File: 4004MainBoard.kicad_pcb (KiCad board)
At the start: 2 copper layers, 95.1 x 72.1 mm, 99 parts, among them J1 BUS, J2 P0 RAM1, J3 CMRAM RAM2, J4 P0 RAM2, J5 DC 5V, Q1 2SA1162GR, Q10 2SC2712GR, Q11 2SA1162GR, Q2 2SC2712GR, Q3 2SA1162GR, Q4 2SC2712GR, Q5 2SA1162GR, Q6 2SA1162GR, Q7 2SA1162GR, Q8 2SA1162GR, Q9 2SC2712GR, SW1 TEST, SW2 RESET, SW3 POWER, U1 74HC08, U2 74HC161, U3 PST600, U4 Intel4004, U5 LT1931A, U6 74LS540, U7 Intel4002-1, U8 Intel4002-1, U9 LT1763, Y1 DLO555MB

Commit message: パターン修正 ビア実装
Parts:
- added R29: 22, Resistors_SMD:R_0603_HandSoldering, B.Cu at (162.1, 111.3)
- added R30: 22, Resistors_SMD:R_0603_HandSoldering, B.Cu at (168.0, 106.4)
- added R31: 22k, Resistors_SMD:R_0603_HandSoldering, B.Cu at (179.3, 101.6)
- added R32: 22k, Resistors_SMD:R_0603_HandSoldering, B.Cu at (198.6, 101.3)
- added R33: 22k, Resistors_SMD:R_0603_HandSoldering, B.Cu at (200.7, 100.7)
- added R34: 22k, Resistors_SMD:R_0603_HandSoldering, B.Cu at (193.4, 101.7)
- added REF**: VIA-0.8-Hole-0.4mm, cd_device:VIA-0.8-Hole-0.4mm, F.Cu at (150.7, 114.2)
- added REF**: VIA-0.8-Hole-0.4mm, cd_device:VIA-0.8-Hole-0.4mm, F.Cu at (157.9, 127.8)
- added REF**: VIA-0.8-Hole-0.4mm, cd_device:VIA-0.8-Hole-0.4mm, F.Cu at (169.9, 134.9)
- added REF**: VIA-0.8-Hole-0.4mm, cd_device:VIA-0.8-Hole-0.4mm, F.Cu at (170.1, 126.1)
- added REF**: VIA-0.8-Hole-0.4mm, cd_device:VIA-0.8-Hole-0.4mm, F.Cu at (168.4, 121.5)
- added REF**: VIA-0.8-Hole-0.4mm, cd_device:VIA-0.8-Hole-0.4mm, F.Cu at (176.4, 137.4)
- added REF**: VIA-0.8-Hole-0.4mm, cd_device:VIA-0.8-Hole-0.4mm, F.Cu at (132.8, 125.7)
- added REF**: VIA-0.8-Hole-0.4mm, cd_device:VIA-0.8-Hole-0.4mm, F.Cu at (142.6, 141.9)
- added REF**: VIA-0.8-Hole-0.4mm, cd_device:VIA-0.8-Hole-0.4mm, F.Cu at (153.3, 133.5)
- added REF**: VIA-0.8-Hole-0.4mm, cd_device:VIA-0.8-Hole-0.4mm, F.Cu at (149.1, 117.6)
- added REF**: VIA-0.8-Hole-0.4mm, cd_device:VIA-0.8-Hole-0.4mm, F.Cu at (146.2, 96.4)
- added REF**: VIA-0.8-Hole-0.4mm, cd_device:VIA-0.8-Hole-0.4mm, F.Cu at (150.7, 138.7)
- added REF**: VIA-0.8-Hole-0.4mm, cd_device:VIA-0.8-Hole-0.4mm, F.Cu at (150.0, 100.2)
- added REF**: VIA-0.8-Hole-0.4mm, cd_device:VIA-0.8-Hole-0.4mm, F.Cu at (139.2, 105.8)
- added REF**: VIA-0.8-Hole-0.4mm, cd_device:VIA-0.8-Hole-0.4mm, F.Cu at (145.7, 85.6)
- added REF**: VIA-0.8-Hole-0.4mm, cd_device:VIA-0.8-Hole-0.4mm, F.Cu at (156.8, 95.4)
- added REF**: VIA-0.8-Hole-0.4mm, cd_device:VIA-0.8-Hole-0.4mm, F.Cu at (174.6, 101.2)
- added REF**: VIA-0.8-Hole-0.4mm, cd_device:VIA-0.8-Hole-0.4mm, F.Cu at (164.3, 95.1)
- added REF**: VIA-0.8-Hole-0.4mm, cd_device:VIA-0.8-Hole-0.4mm, F.Cu at (162.2, 79.5)
- added REF**: VIA-0.8-Hole-0.4mm, cd_device:VIA-0.8-Hole-0.4mm, F.Cu at (208.3, 81.3)
- added REF**: VIA-0.8-Hole-0.4mm, cd_device:VIA-0.8-Hole-0.4mm, F.Cu at (203.5, 90.7)
- added REF**: VIA-0.8-Hole-0.4mm, cd_device:VIA-0.8-Hole-0.4mm, F.Cu at (196.8, 85.2)
- added REF**: VIA-0.8-Hole-0.4mm, cd_device:VIA-0.8-Hole-0.4mm, F.Cu at (148.1, 138.7)
- added REF**: VIA-0.8-Hole-0.4mm, cd_device:VIA-0.8-Hole-0.4mm, F.Cu at (180.2, 131.1)
- added REF**: VIA-0.8-Hole-0.4mm, cd_device:VIA-0.8-Hole-0.4mm, F.Cu at (225.0, 81.2)
- added REF**: VIA-0.8-Hole-0.4mm, cd_device:VIA-0.8-Hole-0.4mm, F.Cu at (218.3, 90.6)
- added REF**: VIA-0.8-Hole-0.4mm, cd_device:VIA-0.8-Hole-0.4mm, F.Cu at (172.8, 84.7)
- added REF**: VIA-0.8-Hole-0.4mm, cd_device:VIA-0.8-Hole-0.4mm, F.Cu at (204.3, 78.9)
- added REF**: VIA-0.8-Hole-0.4mm, cd_device:VIA-0.8-Hole-0.4mm, F.Cu at (193.3, 91.7)
- added REF**: VIA-0.8-Hole-0.4mm, cd_device:VIA-0.8-Hole-0.4mm, F.Cu at (215.1, 72.5)
- added REF**: VIA-0.8-Hole-0.4mm, cd_device:VIA-0.8-Hole-0.4mm, F.Cu at (190.1, 142.0)
- added REF**: VIA-0.8-Hole-0.4mm, cd_device:VIA-0.8-Hole-0.4mm, F.Cu at (225.3, 120.1)
- added REF**: VIA-0.8-Hole-0.4mm, cd_device:VIA-0.8-Hole-0.4mm, F.Cu at (225.3, 135.8)
- added REF**: VIA-0.8-Hole-0.4mm, cd_device:VIA-0.8-Hole-0.4mm, F.Cu at (145.5, 108.0)
- added REF**: VIA-0.8-Hole-0.4mm, cd_device:VIA-0.8-Hole-0.4mm, F.Cu at (196.6, 130.7)
- added REF**: VIA-0.8-Hole-0.4mm, cd_device:VIA-0.8-Hole-0.4mm, F.Cu at (219.1, 141.9)
- added REF**: VIA-0.8-Hole-0.4mm, cd_device:VIA-0.8-Hole-0.4mm, F.Cu at (223.8, 116.0)
- added REF**: VIA-0.8-Hole-0.4mm, cd_device:VIA-0.8-Hole-0.4mm, F.Cu at (212.2, 124.1)
- added REF**: VIA-0.8-Hole-0.4mm, cd_device:VIA-0.8-Hole-0.4mm, F.Cu at (214.8, 118.6)
- added REF**: VIA-0.8-Hole-0.4mm, cd_device:VIA-0.8-Hole-0.4mm, F.Cu at (205.4, 105.3)
- added REF**: VIA-0.8-Hole-0.4mm, cd_device:VIA-0.8-Hole-0.4mm, F.Cu at (207.0, 115.7)
- added REF**: VIA-0.8-Hole-0.4mm, cd_device:VIA-0.8-Hole-0.4mm, F.Cu at (185.4, 87.8)
- added REF**: VIA-0.8-Hole-0.4mm, cd_device:VIA-0.8-Hole-0.4mm, F.Cu at (175.5, 119.5)
- added REF**: VIA-0.8-Hole-0.4mm, cd_device:VIA-0.8-Hole-0.4mm, F.Cu at (182.8, 116.1)
- added REF**: VIA-0.8-Hole-0.4mm, cd_device:VIA-0.8-Hole-0.4mm, F.Cu at (140.6, 109.7)
- added REF**: VIA-0.8-Hole-0.4mm, cd_device:VIA-0.8-Hole-0.4mm, F.Cu at (196.5, 118.9)
- added REF**: VIA-0.8-Hole-0.4mm, cd_device:VIA-0.8-Hole-0.4mm, F.Cu at (145.4, 123.7)
- added REF**: VIA-0.8-Hole-0.4mm, cd_device:VIA-0.8-Hole-0.4mm, F.Cu at (141.1, 114.8)
- added REF**: VIA-0.8-Hole-0.4mm, cd_device:VIA-0.8-Hole-0.4mm, F.Cu at (139.3, 123.7)
- added REF**: VIA-0.8-Hole-0.4mm, cd_device:VIA-0.8-Hole-0.4mm, F.Cu at (147.1, 131.4)
- D12: value POWER LED -> POWER
- R13: value 10 -> 22
- moved C18 0.80 mm to (196.5, 115.3), turned to 90 degrees
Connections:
- Q2 pad 2: /CLK2 -> Net-(Q2-Pad2)
- Q4 pad 2: /CLK1 -> Net-(Q4-Pad2)
- Q5 pad 2: /CLK2 -> Net-(Q2-Pad2)
- Q6 pad 2: /CLK1 -> Net-(Q4-Pad2)
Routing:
- net GND: track 3.36 -> 30.7 mm
- net VCC: track 361.9 -> 381.3 mm, vias 8 -> 9
- net /CLK2: track 102.5 -> 93.9 mm
- net /D0: track 59.8 -> 68.0 mm
- net Net-(Q2-Pad2): track 0.00 -> 6.39 mm
- net /D1: track 66.8 -> 73.0 mm
- net Net-(C20-Pad1): track 24.9 -> 30.7 mm, vias 2 -> 3
- net Net-(Q4-Pad2): track 0.00 -> 3.50 mm
- net /D2: track 70.8 -> 74.2 mm
- net /CLK1: track 86.7 -> 84.3 mm
- net Net-(J1-Pad32): track 67.5 -> 65.6 mm
- net Net-(D1-Pad1): track 0.00 -> 1.49 mm, vias 0 -> 1
- net Net-(J1-Pad31): track 59.5 -> 58.0 mm
- net Net-(D6-Pad1): track 0.00 -> 1.33 mm, vias 0 -> 1
- net Net-(D7-Pad1): track 0.00 -> 1.32 mm, vias 0 -> 1
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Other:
- board text added: "1"

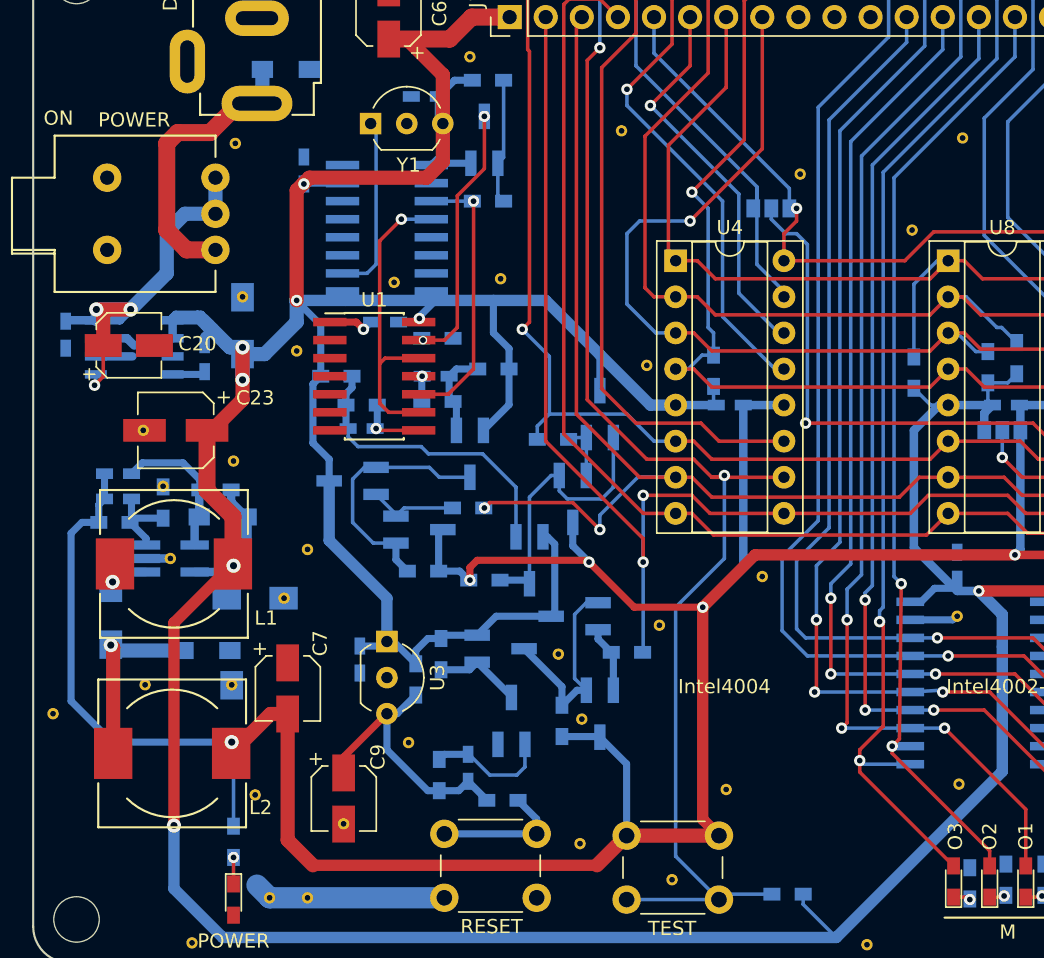
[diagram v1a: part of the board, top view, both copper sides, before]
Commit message: 回路修正 シルク修正
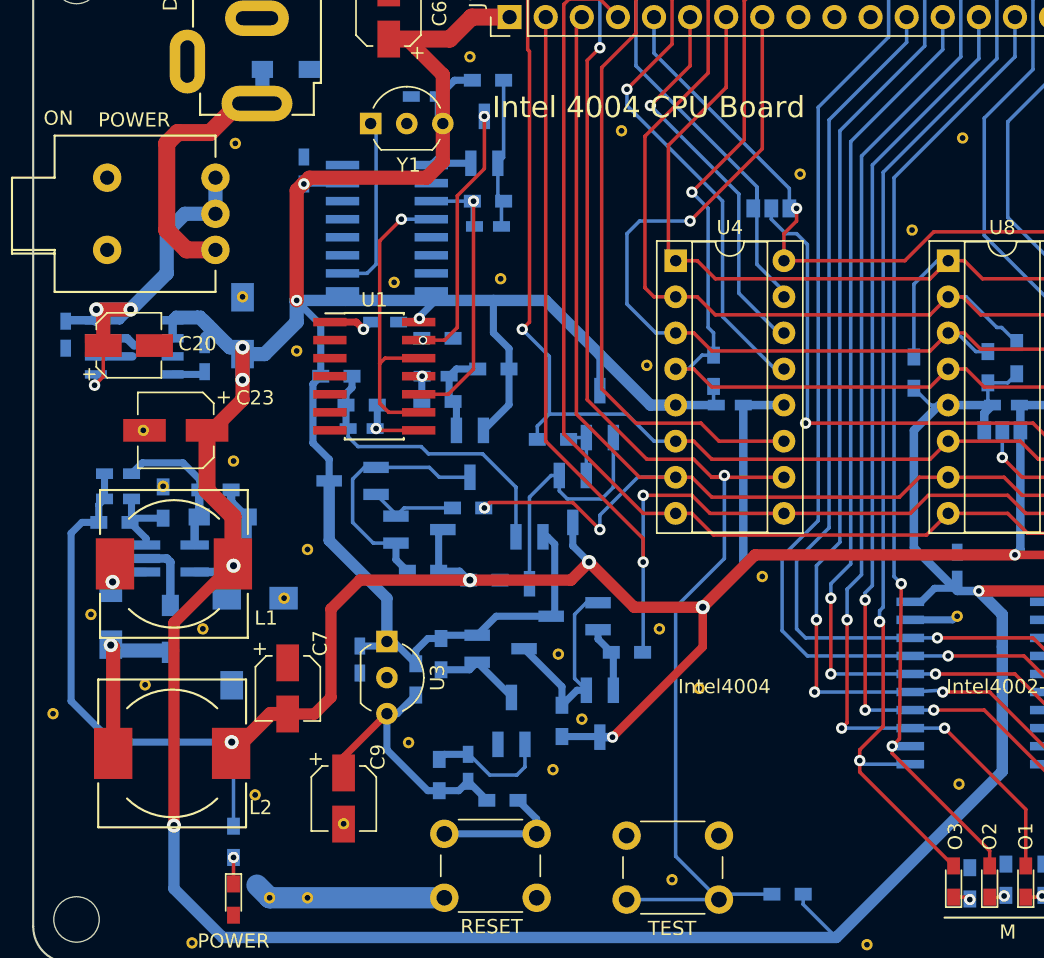
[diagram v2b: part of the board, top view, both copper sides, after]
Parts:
- added C25: 100p, Capacitors_SMD:C_0603_HandSoldering, B.Cu at (163.4, 91.4)
- moved REF** 7.36 mm to (178.3, 124.0)
- moved REF** 6.84 mm to (135.5, 118.7)
- moved REF** 5.54 mm to (168.0, 129.7)
- moved REF** 4.43 mm to (143.4, 119.8)
- moved D3 2.96 mm to (141.1, 119.8), turned to 270 degrees
- moved REF** 0.25 mm to (175.5, 119.8)
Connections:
- SW1 pad 2: /-10V -> GND
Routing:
- net /-10V: track 271.0 -> 238.4 mm, vias 5 -> 6
- net GND: track 30.7 -> 33.9 mm
- net Net-(C25-Pad1): track 8.84 -> 10.7 mm
- net Net-(C25-Pad2): track 19.4 -> 21.2 mm
- net VCC: track 381.3 -> 382.1 mm
- net Net-(C10-Pad1): track 13.0 -> 12.2 mm
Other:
- board text added: "2018-05-13"
- board text added: "Intel 4004 CPU Board"

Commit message: 微調整
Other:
- board text added: "RAM1"
- board text added: "RAM2"
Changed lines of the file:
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@@
     (area 131.369999 71.044999 226.643001 143.331001)
     (thickness 1.6)
-    (drawings 50)
+    (drawings 53)
     (tracks 945)
     (zones 0)
@@
     (aux_axis_origin 0 0)
     (grid_origin 198.882 95.885)
-    (visible_elements FFFFFF5F)
+    (visible_elements FFFFFF7F)
     (pcbplotparams
       (layerselection 0x00030_80000001)
@@
     (descr "Through hole straight pin header, 2x20, 2.54mm pitch, double rows")
     (tags "Through hole pin header THT 2x20 2.54mm double row")
-    (fp_text reference J1 (at 1.27 -2.33 90) (layer F.SilkS)
+    (fp_text reference J1 (at 2.921 -2.921 90) (layer F.SilkS)
       (effects (font (size 1 1) (thickness 0.15)))
     )
@@
     (descr "16-lead though-hole mounted DIP package, row spacing 7.62 mm (300 mils), Socket")
     (tags "THT DIP DIL PDIP 2.54mm 7.62mm 300mil Socket")
-    (fp_text reference U4 (at 3.81 -2.33) (layer F.SilkS)
+    (fp_text reference U4 (at 3.683 -7.874) (layer F.SilkS)
       (effects (font (size 1 1) (thickness 0.15)))
     )
@@
     (descr "16-lead though-hole mounted DIP package, row spacing 7.62 mm (300 mils), Socket")
     (tags "THT DIP DIL PDIP 2.54mm 7.62mm 300mil Socket")
-    (fp_text reference U7 (at 3.81 -2.33) (layer F.SilkS)
+    (fp_text reference U7 (at 3.81 -7.874) (layer F.SilkS)
       (effects (font (size 1 1) (thickness 0.15)))
     )
@@
     (descr "16-lead though-hole mounted DIP package, row spacing 7.62 mm (300 mils), Socket")
     (tags "THT DIP DIL PDIP 2.54mm 7.62mm 300mil Socket")
-    (fp_text reference U8 (at 3.81 -2.33) (layer F.SilkS)
+    (fp_text reference U8 (at 3.81 -7.874) (layer F.SilkS)
       (effects (font (size 1 1) (thickness 0.15)))
     )
@@
     )
   )
+  (gr_line (start 187.833 86.741) (end 228.092 86.741) (angle 90) (layer F.CrtYd) (width 0.15))
+  (gr_text RAM1 (at 218.948 125.476) (layer F.SilkS)
+    (effects (font (size 1 1) (thickness 0.15)))
+  )
+  (gr_text RAM2 (at 199.771 125.476) (layer F.SilkS)
+    (effects (font (size 1 1) (thickness 0.15)))
+  )
   (gr_text "Intel 4004 CPU Board" (at 174.752 83.058) (layer F.SilkS)

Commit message: 調整
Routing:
- net VCC: track 382.1 -> 385.2 mm, vias 9 -> 10
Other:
- board text added: "*"
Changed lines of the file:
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@@
     (links 331)
     (no_connects 0)
-    (area 131.369999 71.044999 226.643001 143.331001)
+    (area 114.453999 59.563 238.887001 149.225001)
     (thickness 1.6)
-    (drawings 53)
-    (tracks 945)
+    (drawings 76)
+    (tracks 949)
     (zones 0)
     (modules 156)
@@
   )
   (setup
-    (last_trace_width 0.8)
+    (last_trace_width 0.25)
     (user_trace_width 0.4)
     (user_trace_width 0.5)
@@
     (zone_45_only yes)
     (trace_min 0.2)
-    (segment_width 1.2)
+    (segment_width 1)
     (edge_width 0.15)
     (via_size 0.6)
@@
     (visible_elements FFFFFF7F)
     (pcbplotparams
-      (layerselection 0x00030_80000001)
-      (usegerberextensions false)
+      (layerselection 0x010f0_80000001)
+      (usegerberextensions true)
       (excludeedgelayer true)
       (linewidth 0.100000)
@@
       (plotinvisibletext false)
       (padsonsilk false)
-      (subtractmaskfromsilk false)
+      (subtractmaskfromsilk true)
       (outputformat 1)
       (mirror false)
-      (drillshape 1)
+      (drillshape 0)
       (scaleselection 1)
       (outputdirectory 4004-gerber/))
@@
       (effects (font (size 1 1) (thickness 0.15)))
     )
-    (fp_text value BUS (at 1.27 50.59 90) (layer F.SilkS)
+    (fp_text value BUS (at 1.27 51.308 90) (layer F.SilkS)
       (effects (font (size 1 1) (thickness 0.15)))
     )
@@
     (tags "resistor 0603")
     (attr smd)
-    (fp_text reference R17 (at 0 1.45 270) (layer B.SilkS)
+    (fp_text reference R17 (at 3.937 -0.127 270) (layer B.SilkS)
       (effects (font (size 1 1) (thickness 0.15)) (justify mirror))
     )
@@
     (tags "resistor 0603")
     (attr smd)
-    (fp_text reference R18 (at 0 1.45 270) (layer B.SilkS)
+    (fp_text reference R18 (at 3.81 -0.127 270) (layer B.SilkS)
       (effects (font (size 1 1) (thickness 0.15)) (justify mirror))
     )
@@
     (tags "resistor 0603")
     (attr smd)
-    (fp_text reference R19 (at 0 1.45 270) (layer B.SilkS)
+    (fp_text reference R19 (at 3.683 -0.127 270) (layer B.SilkS)
       (effects (font (size 1 1) (thickness 0.15)) (justify mirror))
     )
@@
     (tags "resistor 0603")
     (attr smd)
-    (fp_text reference R21 (at 0 1.45 270) (layer B.SilkS)
+    (fp_text reference R21 (at 3.683 -0.127 270) (layer B.SilkS)
       (effects (font (size 1 1) (thickness 0.15)) (justify mirror))
     )
@@
     (tags "resistor 0603")
     (attr smd)
-    (fp_text reference R22 (at 0 1.45 270) (layer B.SilkS)
+    (fp_text reference R22 (at 3.683 0 270) (layer B.SilkS)
       (effects (font (size 1 1) (thickness 0.15)) (justify mirror))
     )
@@
     (tags "resistor 0603")
     (attr smd)
-    (fp_text reference R23 (at 0 1.45 270) (layer B.SilkS)
+    (fp_text reference R23 (at 3.81 0 270) (layer B.SilkS)
       (effects (font (size 1 1) (thickness 0.15)) (justify mirror))
     )
@@
     (tags "resistor 0603")
     (attr smd)
-    (fp_text reference R24 (at 0 1.45 270) (layer B.SilkS)
+    (fp_text reference R24 (at 3.81 0 270) (layer B.SilkS)
       (effects (font (size 1 1) (thickness 0.15)) (justify mirror))
     )
@@
     (tags "resistor 0603")
     (attr smd)
-    (fp_text reference R26 (at 0 1.45 270) (layer B.SilkS)
+    (fp_text reference R26 (at 3.556 0 270) (layer B.SilkS)
       (effects (font (size 1 1) (thickness 0.15)) (justify mirror))
     )
@@
       (effects (font (size 1 1) (thickness 0.15)) (justify mirror))
     )
-    (fp_text value TEST (at 3.302 -2.032 180) (layer F.SilkS)
+    (fp_text value TEST (at 3.302 -2.413 180) (layer F.SilkS)
       (effects (font (size 1 1) (thickness 0.15)))
     )
@@
       (effects (font (size 1 1) (thickness 0.15)) (justify mirror))
     )
-    (fp_text value RESET (at 3.175 -2.032 180) (layer F.SilkS)
+    (fp_text value RESET (at 3.175 -2.54 180) (layer F.SilkS)
       (effects (font (size 1 1) (thickness 0.15)))
     )
@@
     )
   )
+  (gr_line (start 144.272 90.551) (end 144.272 88.011) (angle 90) (layer B.Mask) (width 1))
+  (gr_line (start 142.113 90.551) (end 144.272 90.551) (angle 90) (layer B.Mask) (width 1))
+  (gr_line (start 140.843 91.821) (end 142.113 90.551) (angle 90) (layer B.Mask) (width 1))
+  (gr_line (start 140.843 94.742) (end 140.843 91.821) (angle 90) (layer B.Mask) (width 1))
+  (gr_line (start 138.303 97.282) (end 140.843 94.742) (angle 90) (layer B.Mask) (width 1))
+  (gr_line (start 149.987 98.171) (end 149.987 94.869) (angle 90) (layer B.Mask) (width 1))
+  (gr_line (start 147.701 100.457) (end 149.987 98.171) (angle 90) (layer B.Mask) (width 1))
+  (gr_line (start 146.177 100.457) (end 147.701 100.457) (angle 90) (layer B.Mask) (width 1))
+  (gr_line (start 146.177 102.235) (end 146.177 99.949) (angle 90) (layer B.Mask) (width 1))
+  (gr_line (start 148.082 138.684) (end 150.749 138.684) (angle 90) (layer B.Mask) (width 1.5))
+  (gr_text * (at 139.573 117.983) (layer B.SilkS)
+    (effects (font (size 1 1) (thickness 0.15)) (justify mirror))
+  )
+  (gr_text * (at 138.938 117.221) (layer B.SilkS)
+    (effects (font (size 1 1) (thickness 0.15)) (justify mirror))
+  )
+  (gr_text * (at 141.224 96.901) (layer B.SilkS)
+    (effects (font (size 1 1) (thickness 0.15)) (justify mirror))
+  )
+  (gr_line (start 137.541 98.044) (end 135.128 98.044) (angle 90) (layer B.Mask) (width 0.6))
+  (gr_line (start 138.303 97.282) (end 137.541 98.044) (angle 90) (layer B.Mask) (width 0.6))
+  (gr_line (start 138.303 97.282) (end 135.89 97.282) (angle 90) (layer B.Mask) (width 1))
+  (gr_line (start 135.89 97.282) (end 135.89 97.79) (angle 90) (layer B.Mask) (width 1))
+  (gr_line (start 142.24 93.091) (end 144.272 93.091) (angle 90) (layer F.Mask) (width 1.2))
+  (gr_line (start 140.843 91.694) (end 142.24 93.091) (angle 90) (layer F.Mask) (width 1.2))
+  (gr_line (start 140.843 85.598) (end 140.843 91.694) (angle 90) (layer F.Mask) (width 1.2))
+  (gr_line (start 141.605 84.836) (end 140.843 85.598) (angle 90) (layer F.Mask) (width 1.2))
+  (gr_line (start 143.891 84.836) (end 141.605 84.836) (angle 90) (layer F.Mask) (width 1.2))
+  (gr_line (start 145.923 82.804) (end 143.891 84.836) (angle 90) (layer F.Mask) (width 1.2))
   (gr_line (start 187.833 86.741) (end 228.092 86.741) (angle 90) (layer F.CrtYd) (width 0.15))
   (gr_text RAM1 (at 218.948 125.476) (layer F.SilkS)
@@
   (gr_arc (start 224.028 140.716) (end 226.568 140.716) (angle 90) (layer Edge.Cuts) (width 0.15))
   (gr_arc (start 224.028 73.66) (end 224.028 71.12) (angle 90) (layer Edge.Cuts) (width 0.15))
+  (segment (start 149.987 98.044) (end 149.987 94.996) (width 1) (layer B.Cu) (net 1))
+  (via (at 149.987 94.996) (size 0.8) (drill 0.4) (layers F.Cu B.Cu) (net 1))
   (segment (start 196.469 116.266) (end 196.469 116.906) (width 0.25) (layer B.Cu) (net 1))
   (segment (start 196.469 116.906) (end 196.469 117.094) (width 0.25) (layer B.Cu) (net 1))
@@
   (via (at 146.177 102.235) (size 1) (drill 0.5) (layers F.Cu B.Cu) (net 1))
   (segment (start 146.177 100.425) (end 147.733 100.425) (width 1) (layer B.Cu) (net 1))
-  (segment (start 149.987 98.171) (end 149.987 96.647) (width 1) (layer B.Cu) (net 1))
+  (segment (start 149.987 98.171) (end 149.987 98.044) (width 1) (layer B.Cu) (net 1))
+  (segment (start 149.987 98.044) (end 149.987 96.647) (width 1) (layer B.Cu) (net 1))
   (segment (start 147.733 100.425) (end 149.987 98.171) (width 1) (layer B.Cu) (net 1))
   (segment (start 144.018 98.679) (end 145.034 99.695) (width 1) (layer B.Cu) (net 1))
@@
   (segment (start 149.971 96.631) (end 149.955 96.647) (width 1) (layer B.Cu) (net 1))
   (segment (start 150.4315 88.4555) (end 149.987 88.9) (width 1) (layer F.Cu) (net 1))
-  (segment (start 149.987 88.9) (end 149.987 96.647) (width 1) (layer F.Cu) (net 1))
+  (segment (start 149.987 88.9) (end 149.987 94.996) (width 1) (layer F.Cu) (net 1))
+  (segment (start 149.987 94.996) (end 149.987 96.647) (width 1) (layer F.Cu) (net 1))
   (via (at 149.987 96.647) (size 0.8) (drill 0.4) (layers F.Cu B.Cu) (net 1))
   (segment (start 149.987 96.647) (end 149.971 96.631) (width 1) (layer B.Cu) (net 1))
